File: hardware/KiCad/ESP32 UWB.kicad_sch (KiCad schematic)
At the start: 55 parts, among them J1 HEADER-20P-2.54, J2 HEADER-12P-2.54, J3 10118194-0001LF, Q1 S8050, Q2 S8050, SW1 BUTTON, SW2 BUTTON, U1 AMS1117-3.3, U2 ESP32-C3-MINI-1-N4, U3 SILICON_LABS_CP2102N-A01-GQFN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, U4 DWM1000

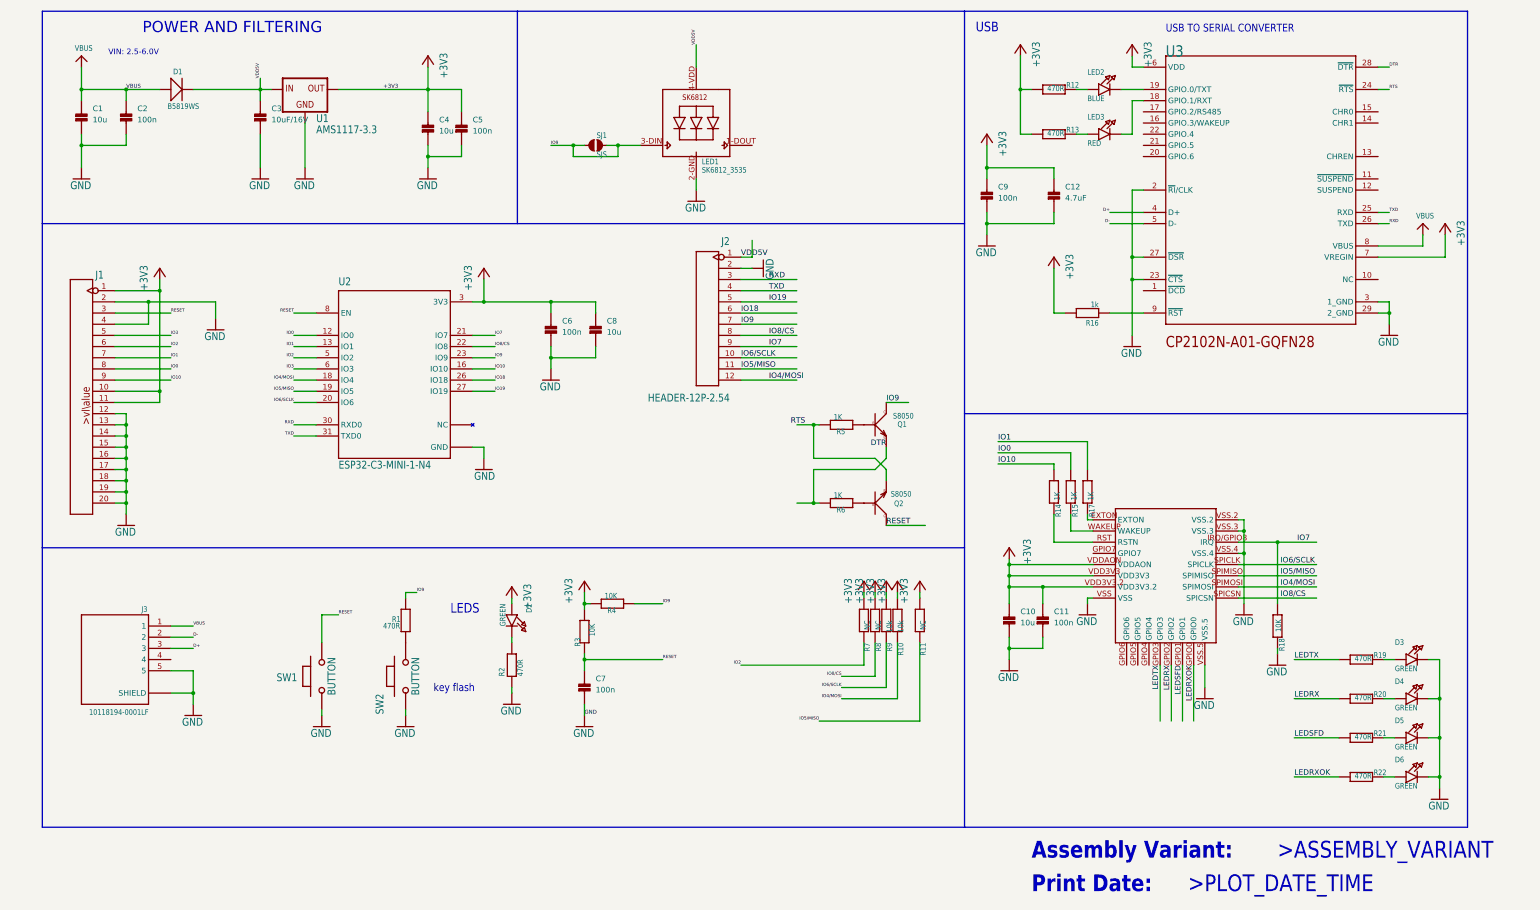
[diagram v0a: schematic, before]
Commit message: update schematic to use built-in kicad symbols
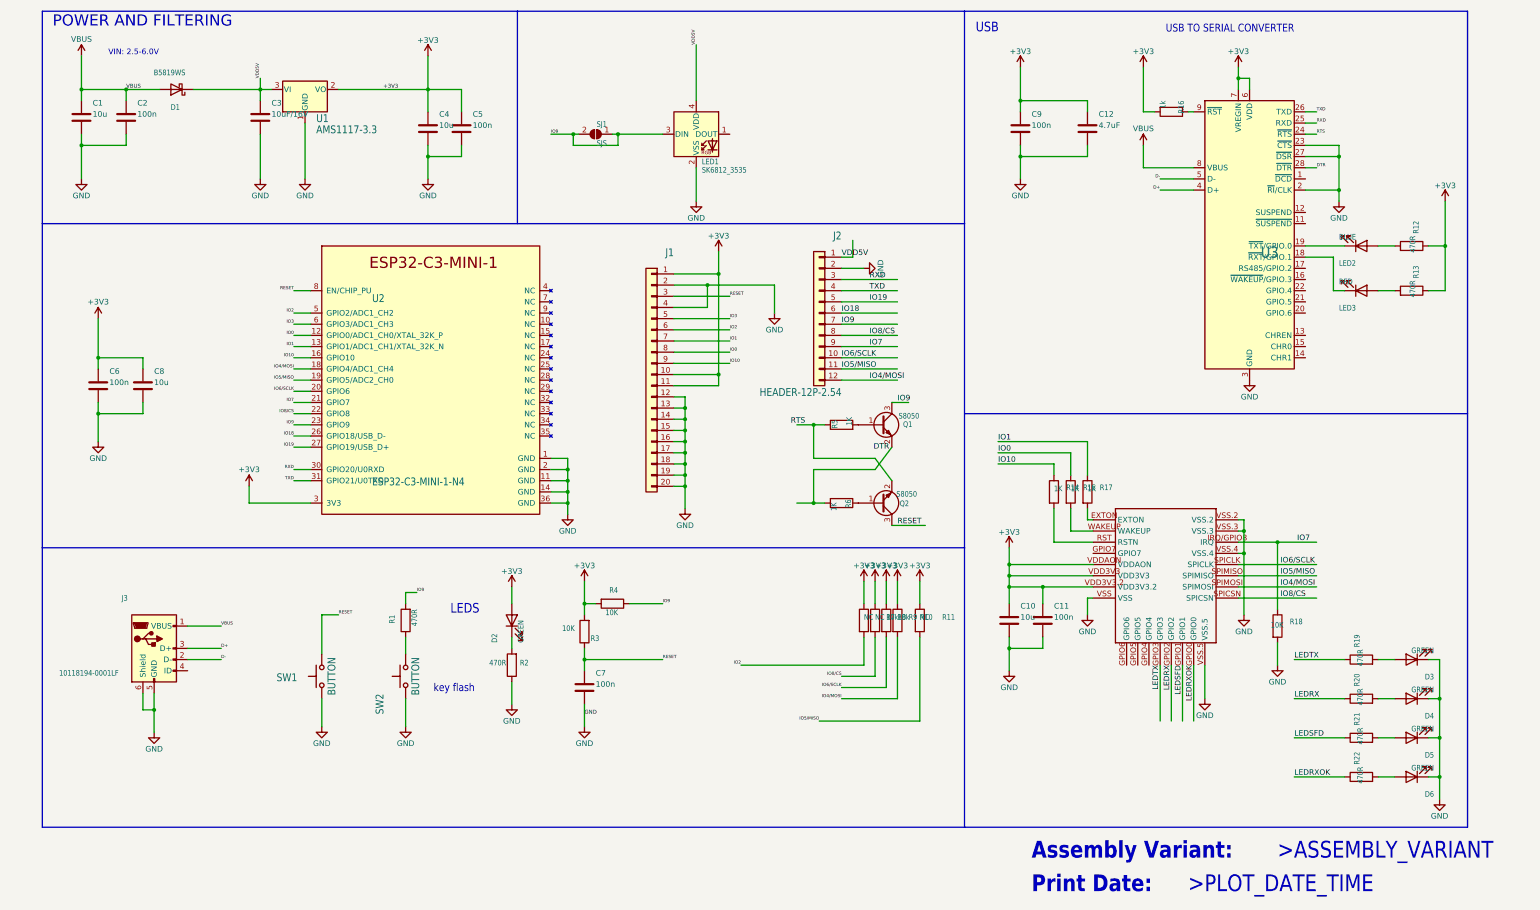
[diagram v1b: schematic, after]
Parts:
- C1, C10, C11, C12, C2, C3, C4, C5, C6, C7, C8, C9: symbol ESP32 UWB-eagle-import:CAP_CERAMIC0603 -> Device:C
- D1: symbol ESP32 UWB-eagle-import:D'0805' -> Device:D_Schottky
- D2, D3, D4, D5, D6: symbol ESP32 UWB-eagle-import:LED0805_NOOUTLINE -> Device:LED
- J1: symbol ESP32 UWB-eagle-import:HEADER-20P-2.54 -> Connector_Generic:Conn_01x20
- J2: symbol ESP32 UWB-eagle-import:HEADER-12P-2.54 -> Connector_Generic:Conn_01x12
- J3: symbol ESP32 UWB-eagle-import:10118194-0001LF -> Connector:USB_B_Micro
- LED1: symbol ESP32 UWB-eagle-import:SK6812_3535 -> LED:SK6812MINI
- LED2, LED3: symbol ESP32 UWB-eagle-import:LED0603_NOOUTLINE -> Device:LED
- Q1, Q2: symbol ESP32 UWB-eagle-import:TRANSISTOR-NPN-SOT23 -> Device:Q_NPN_BEC
- R1, R10, R11, R12, R13, R14, R15, R16, R17, R18, R19, R2, R20, R21, R22, R3, R4, R5, R6, R7, R8, R9: symbol ESP32 UWB-eagle-import:RESISTOR0603 -> Device:R
- SJ1: symbol ESP32 UWB-eagle-import:SJS -> Jumper:SolderJumper_2_Open
- SW1, SW2: symbol ESP32 UWB-eagle-import:PB157 -> Switch:SW_Push
- U1: symbol ESP32 UWB-eagle-import:V_REG_MIC2920 -> Regulator_Linear:AMS1117-3.3
- U2: symbol ESP32 UWB-eagle-import:ESP32-C3-MINI-1-N4 -> Espressif:ESP32-C3-MINI-1
- U3: symbol ESP32 UWB-eagle-import:SILICON_LABS_CP2102N-A01-GQFN28SILICON_LABS_CP2102N-A01-GQFN28_0_3 -> Interface_USB:CP2102N-Axx-xQFN28
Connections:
- net +3V3: now also D2.2 (A), U1.2 (VO); no longer D2.A, U1.3 (OUT)
- net GND: now also D3.1 (K), D4.1 (K), D5.1 (K), D6.1 (K), J3.6 (Shield), LED1.2 (VSS), U1.1 (GND); no longer D3.C, D4.C, D5.C, D6.C, J3.S1 (SHIELD), J3.S2 (SHIELD), J3.S3 (SHIELD), J3.S4 (SHIELD), J3.S5 (SHIELD), J3.S6 (SHIELD), LED1.2-GND (GND), U1.2 (GND), U2.37 (GND), U2.38 (GND), U2.39 (GND), U2.40 (GND), U2.41 (GND), U2.42 (GND), U2.43 (GND), U2.44 (GND), U2.45 (GND), U2.46 (GND), U2.47 (GND), U2.48 (GND), U2.49_1 (GND), U2.49_2 (GND), U2.49_3 (GND), U2.49_4 (GND), U2.49_5 (GND), U2.49_6 (GND), U2.49_7 (GND), U2.49_8 (GND), U2.49_9 (GND), U2.50 (GND), U2.51 (GND), U2.52 (GND), U2.53 (GND)
- net IO8/CS: no longer U2.22 (IO8)
- net IO9: now also LED1.3 (DIN); no longer LED1.3-DIN (DI)
- net RTS: now also R5.1; no longer R5.2
- net RXD: now also U3.25 (RXD); no longer U3.26 (TXD)
- net TXD: now also U3.26 (TXD); no longer U3.25 (RXD)
- net VBUS: now also D1.2 (A); no longer D1.+
- net VDD5V: now also D1.1 (K), LED1.4 (VDD), U1.3 (VI); no longer D1.-, LED1.4-VDD (VDD), U1.1 (IN)
- net at R2.2: now also D2.1 (K); no longer D2.C
- net at R13.2: now also LED3.2 (A); no longer LED3.A
- net at U3.18 (~{RXT}/GPIO.1): now also LED3.1 (K); no longer LED3.C
- net at U3.19 (~{TXT}/GPIO.0): now also LED2.1 (K); no longer LED2.C
- net at R19.2: now also D3.2 (A); no longer D3.A
- net at R12.2: now also LED2.2 (A); no longer LED2.A
- net at R21.2: now also D5.2 (A); no longer D5.A
- net at R22.2: now also D6.2 (A); no longer D6.A
- net at Q1.1 (B): now also R5.2; no longer R5.1
- net at R20.2: now also D4.2 (A); no longer D4.A
- new net IO8/CS: U2.22 (GPIO8)
- now unconnected: U2.10 (NC), U2.15 (NC), U2.17 (NC), U2.24 (NC), U2.25 (NC), U2.28 (NC), U2.29 (NC), U2.32 (NC), U2.33 (NC), U2.34 (NC), U2.35 (NC), U2.4 (NC), U2.7 (NC), U2.9 (NC)
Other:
- moved on the sheet: Q1, Q2

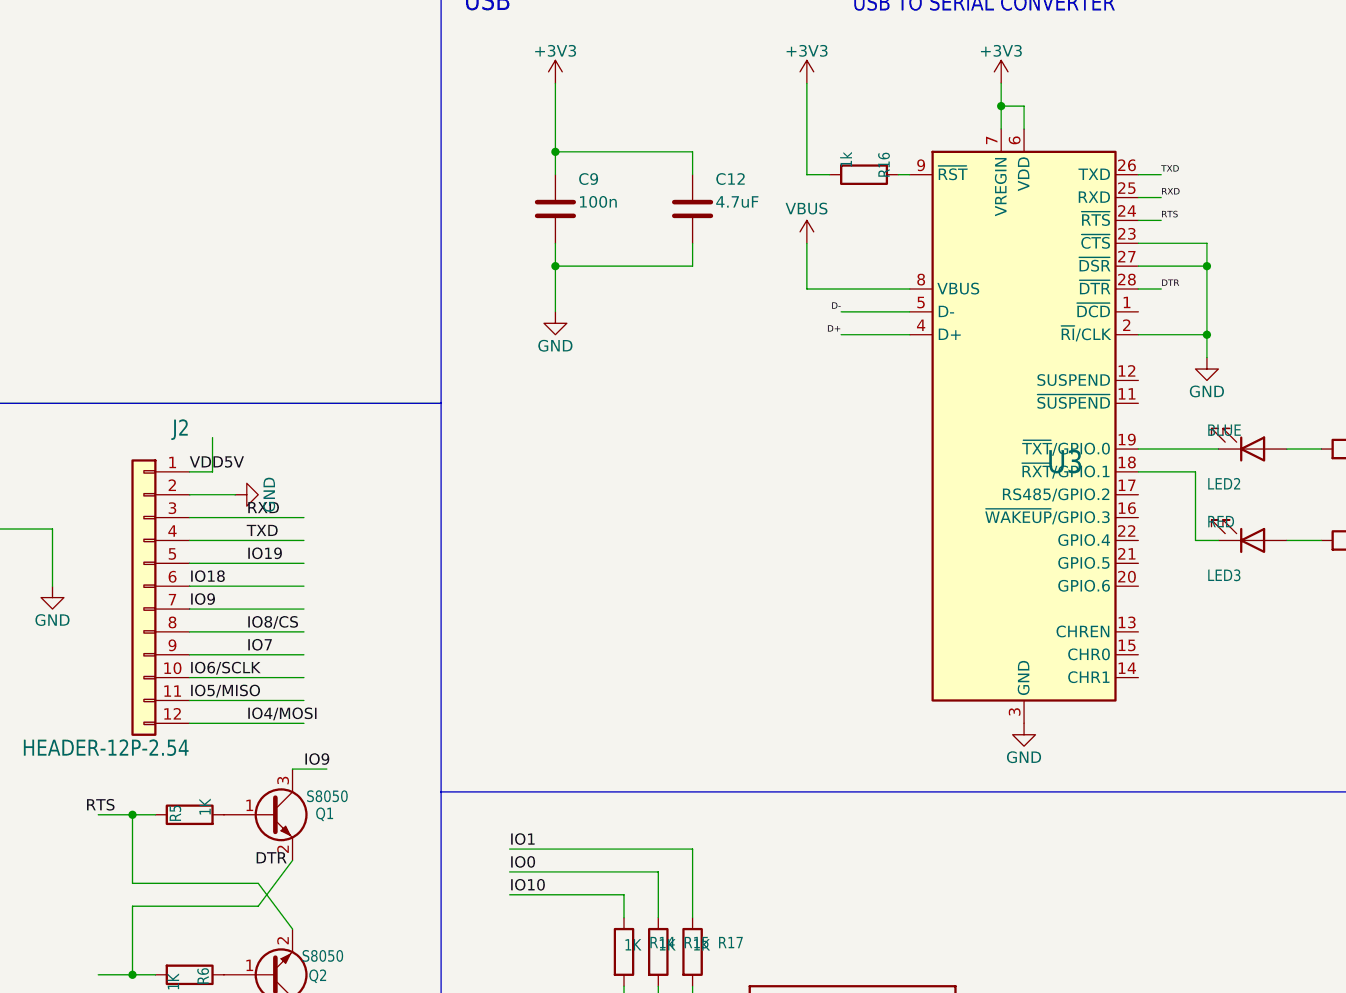
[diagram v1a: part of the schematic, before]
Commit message: change all footprints in schematic
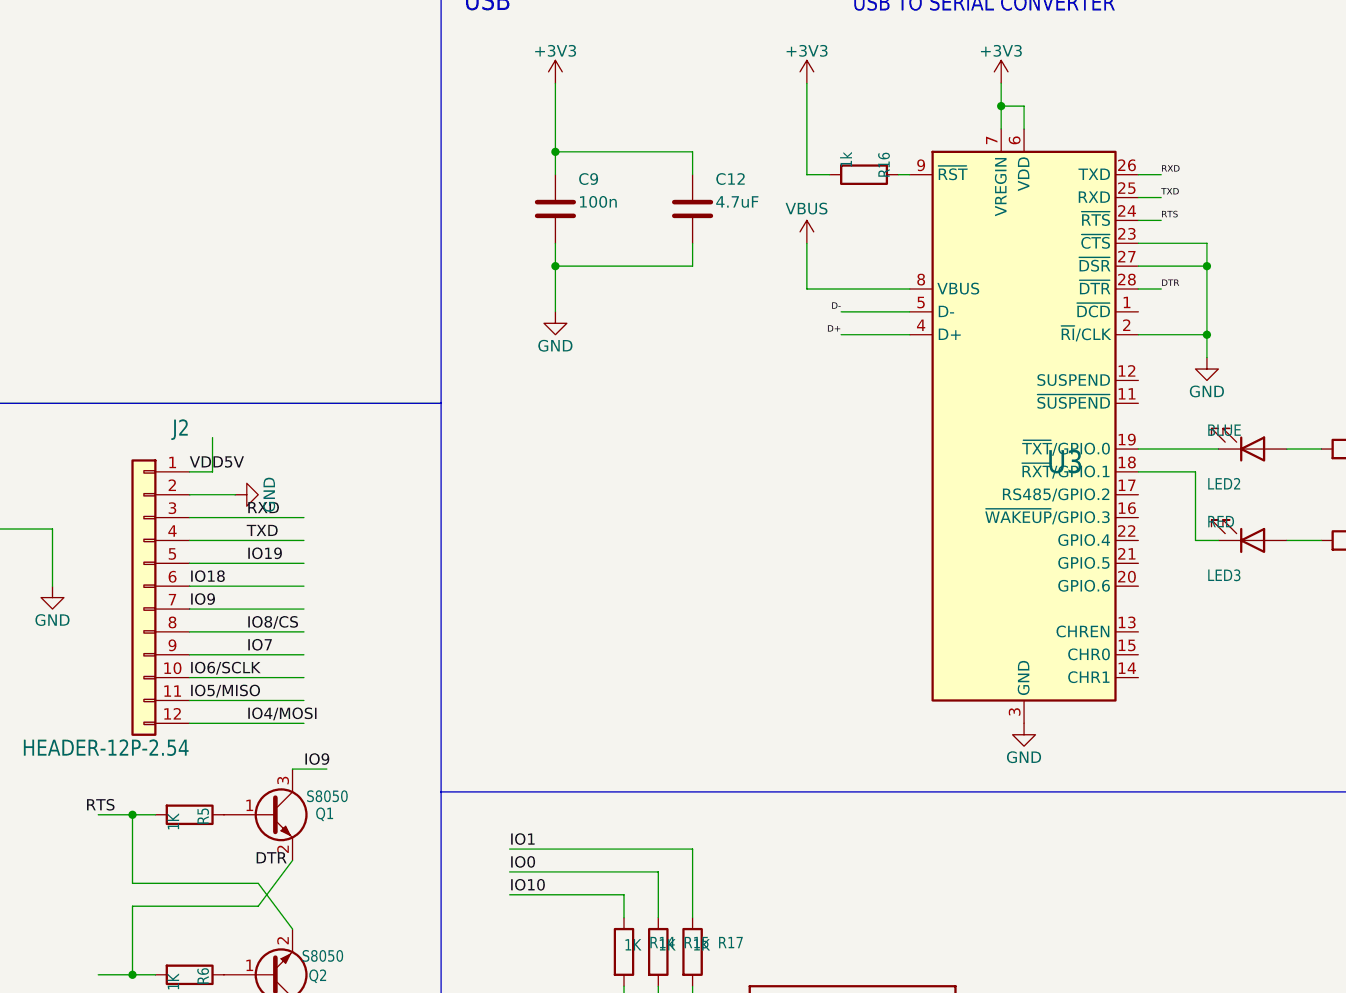
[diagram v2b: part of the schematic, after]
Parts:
- C1, C10, C11, C12, C2, C3, C4, C5, C6, C7, C8, C9: footprint 0603 -> Capacitor_SMD:C_0603_1608Metric_Pad1.08x0.95mm_HandSolder
- D1: footprint SOD323 -> Diode_SMD:D_SOD-323_HandSoldering
- D2, D3, D4, D5, D6: footprint CHIPLED_0805_NOOUTLINE -> LED_SMD:LED_0805_2012Metric_Pad1.15x1.40mm_HandSolder
- J1: footprint 20P-2.54 -> Connector_PinHeader_2.54mm:PinHeader_1x20_P2.54mm_Vertical
- J2: footprint 12P-2.54 -> Connector_PinHeader_2.54mm:PinHeader_1x12_P2.54mm_Vertical
- J3: footprint AMPHENOL_10118194-0001LF -> Connector_USB:USB_Micro-B_Amphenol_10118194_Horizontal
- LED1: footprint LED3535 -> LED_SMD:LED_SK6812MINI_PLCC4_3.5x3.5mm_P1.75mm
- LED2, LED3: footprint CHIPLED_0603_NOOUTLINE -> LED_SMD:LED_0603_1608Metric_Pad1.05x0.95mm_HandSolder
- Q1, Q2: footprint SOT23 -> Package_TO_SOT_SMD:SOT-23
- R1, R10, R11, R12, R13, R14, R15, R16, R17, R18, R19, R2, R20, R21, R22, R3, R4, R5, R6, R7, R8, R9: footprint 0603 -> Resistor_SMD:R_0603_1608Metric_Pad0.98x0.95mm_HandSolder
- SJ1: footprint SJ_S -> Jumper:SolderJumper-2_P1.3mm_Open_TrianglePad1.0x1.5mm
- SW1, SW2: footprint 157SW -> Button_Switch_SMD:SW_Push_SPST_NO_Alps_SKRK
- U1: footprint SOT223 -> Package_TO_SOT_SMD:SOT-223-3_TabPin2
- U2: footprint XCVR_ESP32-C3-MINI-1-N4 -> Espressif:ESP32-C3-MINI-1
- U3: footprint SILICON_LABS_CP2102N-A01-GQFN28_3 -> Package_DFN_QFN:QFN-28-1EP_5x5mm_P0.5mm_EP3.35x3.35mm
- U4: footprint DWM1000 -> ESP32 UWB:DWM1000
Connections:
- net RTS: now also R5.2; no longer R5.1
- net RXD: now also U3.26 (TXD); no longer U3.25 (RXD)
- net TXD: now also U3.25 (RXD); no longer U3.26 (TXD)
- net at Q1.1 (B): now also R5.1; no longer R5.2
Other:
- moved on the sheet: R5

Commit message: fox pcb
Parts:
- U2: footprint Espressif:ESP32-C3-MINI-1 -> Espressif:ESP32-C3-MINI-1_Hand-Soldering
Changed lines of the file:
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@@
       (effects (font (size 1.778 1.5113)) (justify left bottom))
     )
-    (property "Footprint" "Espressif:ESP32-C3-MINI-1" (id 2) (at 109.22 102.87 0)
+    (property "Footprint" "Espressif:ESP32-C3-MINI-1_Hand-Soldering" (id 2) (at 109.22 102.87 0)
       (effects (font (size 1.27 1.27)) hide)
     )
@@
     )
     (path "/bdf9dfdb-3e3e-46cc-8bb8-4372561c164b"
-      (reference "U2") (unit 1) (value "ESP32-C3-MINI-1-N4") (footprint "Espressif:ESP32-C3-MINI-1")
+      (reference "U2") (unit 1) (value "ESP32-C3-MINI-1-N4") (footprint "Espressif:ESP32-C3-MINI-1_Hand-Soldering")
     )
     (path "/44d6780b-0f7d-4066-bfb2-bff50f00afa0"

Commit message: more tweaks
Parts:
- U2: footprint Espressif:ESP32-C3-MINI-1_Hand-Soldering -> Espressif:ESP32-C3-MINI-1
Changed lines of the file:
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@@
       (effects (font (size 1.778 1.5113)) (justify left bottom))
     )
-    (property "Footprint" "Espressif:ESP32-C3-MINI-1_Hand-Soldering" (id 2) (at 109.22 102.87 0)
+    (property "Footprint" "Espressif:ESP32-C3-MINI-1" (id 2) (at 109.22 102.87 0)
       (effects (font (size 1.27 1.27)) hide)
     )
@@
     )
     (path "/bdf9dfdb-3e3e-46cc-8bb8-4372561c164b"
-      (reference "U2") (unit 1) (value "ESP32-C3-MINI-1-N4") (footprint "Espressif:ESP32-C3-MINI-1_Hand-Soldering")
+      (reference "U2") (unit 1) (value "ESP32-C3-MINI-1-N4") (footprint "Espressif:ESP32-C3-MINI-1")
     )
     (path "/44d6780b-0f7d-4066-bfb2-bff50f00afa0"

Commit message: tweak silkscreen and 3d model
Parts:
- U2: footprint Espressif:ESP32-C3-MINI-1 -> Espressif:ESP32-C3-MINI-1_Hand-Soldering
- renumbered C12 to C10, C10 to C12, C5 to C4, C4 to C5, C8 to C7, C7 to C8, D6 to D3, D5 to D4, D3 to D5, D4 to D6, LED2 to D7, LED3 to D8, R3 to R1, R8 to R10, R9 to R11, R11 to R12, R10 to R13, R17 to R16, R16 to R17, R21 to R19, R4 to R2, R22 to R21, R19 to R22, R1 to R3, R2 to R4, R12 to R7, R13 to R8, R7 to R9, LED1 to U5

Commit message: swap pushbuttons
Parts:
- SW1, SW2: footprint Button_Switch_SMD:SW_Push_SPST_NO_Alps_SKRK -> Button_Switch_SMD:SW_SPST_EVQPE1
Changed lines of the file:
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@@
       (effects (font (size 1.778 1.5113)) (justify left bottom))
     )
-    (property "Footprint" "Button_Switch_SMD:SW_Push_SPST_NO_Alps_SKRK" (id 2) (at 104.14 168.91 0)
+    (property "Footprint" "Button_Switch_SMD:SW_SPST_EVQPE1" (id 2) (at 104.14 168.91 0)
       (effects (font (size 1.27 1.27)) hide)
     )
@@
       (effects (font (size 1.778 1.5113)) (justify left bottom))
     )
-    (property "Footprint" "Button_Switch_SMD:SW_Push_SPST_NO_Alps_SKRK" (id 2) (at 85.09 168.91 0)
+    (property "Footprint" "Button_Switch_SMD:SW_SPST_EVQPE1" (id 2) (at 85.09 168.91 0)
       (effects (font (size 1.27 1.27)) hide)
     )
@@
     )
     (path "/26769327-3160-41f1-82e7-11d5d542abde"
-      (reference "SW1") (unit 1) (value "BUTTON") (footprint "Button_Switch_SMD:SW_Push_SPST_NO_Alps_SKRK")
+      (reference "SW1") (unit 1) (value "BUTTON") (footprint "Button_Switch_SMD:SW_SPST_EVQPE1")
     )
     (path "/006bc43b-d3a8-4a38-a8dc-5a24da3f9b4d"
-      (reference "SW2") (unit 1) (value "BUTTON") (footprint "Button_Switch_SMD:SW_Push_SPST_NO_Alps_SKRK")
+      (reference "SW2") (unit 1) (value "BUTTON") (footprint "Button_Switch_SMD:SW_SPST_EVQPE1")
     )
     (path "/713f8bf8-d771-4862-bb18-7b6f3b027ba3"
